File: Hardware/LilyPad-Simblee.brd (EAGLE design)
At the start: 45.3 x 45.2 mm, 37 parts, among them U1 MIC5219 3.3V, U2 MCP73831, U3 RFD77101

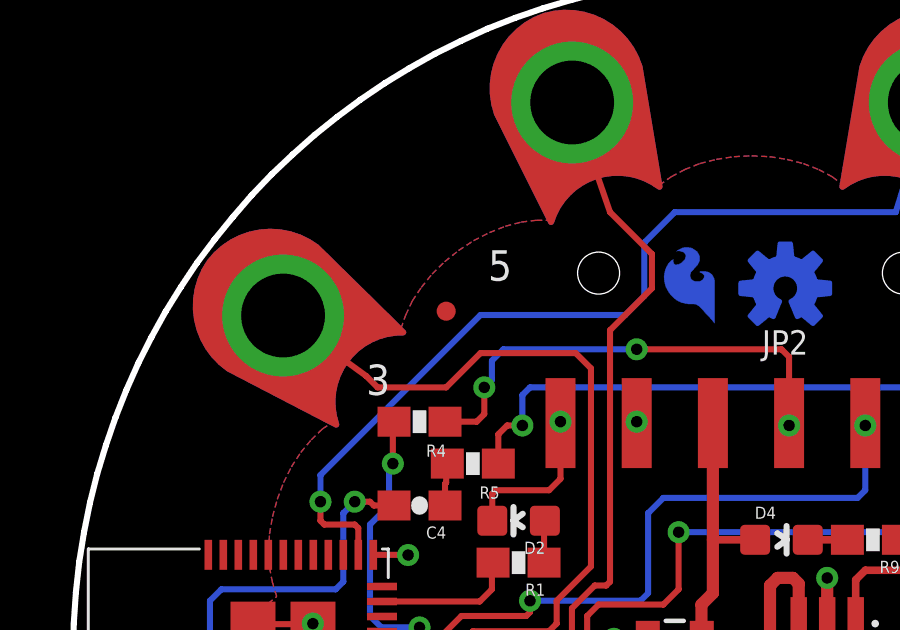
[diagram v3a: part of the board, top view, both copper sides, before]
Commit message: minor movement of fid for better ground pour
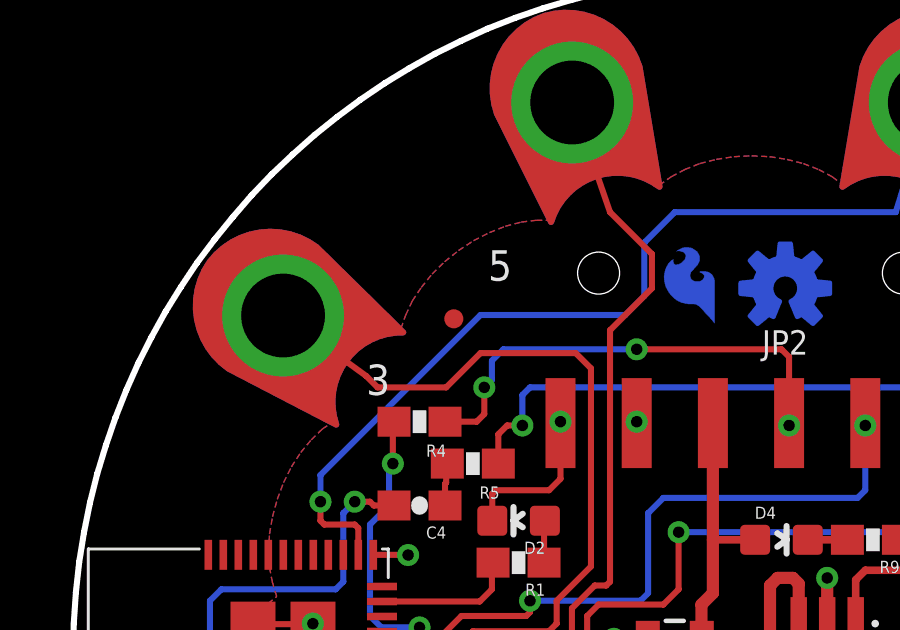
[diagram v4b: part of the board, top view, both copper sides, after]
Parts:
- moved FID1 0.36 mm to (-9.91, 11.2)
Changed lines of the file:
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@@
 <?xml version="1.0" encoding="utf-8"?>
 <!DOCTYPE eagle SYSTEM "eagle.dtd">
-<eagle version="7.3.0">
+<eagle version="7.5.0">
 <drawing>
 <settings>
@@
 <setting verticaltext="up"/>
 </settings>
-<grid distance="0.05" unitdist="inch" unit="inch" style="lines" multiple="1" display="yes" altdistance="0.005" altunitdist="inch" altunit="inch"/>
+<grid distance="0.01" unitdist="inch" unit="inch" style="lines" multiple="1" display="yes" altdistance="0.001" altunitdist="inch" altunit="inch"/>
 <layers>
 <layer number="1" name="Top" color="4" fill="1" visible="yes" active="yes"/>
@@
 <layer number="19" name="Unrouted" color="6" fill="1" visible="yes" active="yes"/>
 <layer number="20" name="Dimension" color="6" fill="1" visible="yes" active="yes"/>
-<layer number="21" name="tPlace" color="16" fill="1" visible="yes" active="yes"/>
-<layer number="22" name="bPlace" color="14" fill="1" visible="yes" active="yes"/>
+<layer number="21" name="tPlace" color="6" fill="1" visible="yes" active="yes"/>
+<layer number="22" name="bPlace" color="6" fill="1" visible="yes" active="yes"/>
 <layer number="23" name="tOrigins" color="15" fill="1" visible="yes" active="yes"/>
 <layer number="24" name="bOrigins" color="15" fill="1" visible="yes" active="yes"/>
@@
 <element name="LOGO1" library="SparkFun-Aesthetics" package="SFE_LOGO_FLAME_COPPER_.1" value="SFE_LOGO_FLAME.1COP" x="-0.889" y="10.668" rot="MR0"/>
 <element name="LOGO2" library="SparkFun-Aesthetics" package="OSHW-LOGO-S_COPPER" value="OSHW-LOGOS-COPPER" x="1.143" y="12.192" rot="MR0"/>
-<element name="FID1" library="SparkFun-Aesthetics" package="MICRO-FIDUCIAL" value="FIDUCIALUFIDUCIAL" x="-10.16" y="11.43"/>
+<element name="FID1" library="SparkFun-Aesthetics" package="MICRO-FIDUCIAL" value="FIDUCIALUFIDUCIAL" x="-9.906" y="11.176"/>
 <element name="FID2" library="SparkFun-Aesthetics" package="MICRO-FIDUCIAL" value="FIDUCIALUFIDUCIAL" x="8.89" y="-12.319"/>
 <element name="U$1" library="LilyPad-Wearables" package="LOGO-L" value="LOGO-LPL" x="9.144" y="6.096"/>
